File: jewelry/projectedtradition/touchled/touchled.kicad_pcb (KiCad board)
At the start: 2 copper layers, 23.6 x 23.6 mm, 18 parts, among them J3 SENSE, Q1 Q_NMOS_GSD, Q2 Q_NMOS_GSD, U1 TPP223-BA6, U2 AP3019A

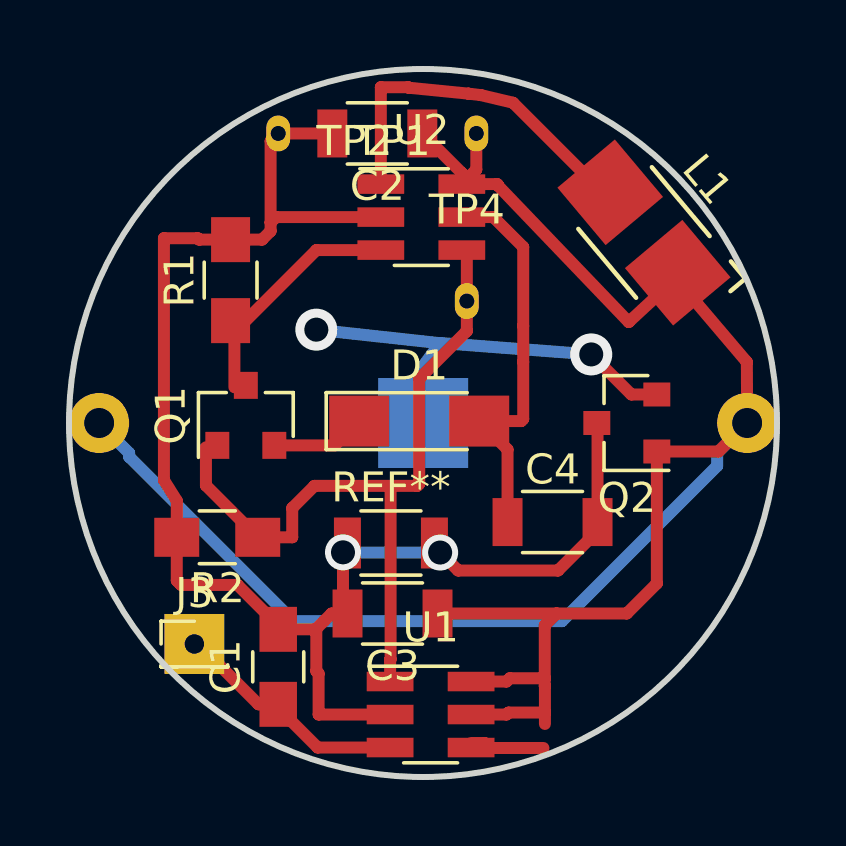
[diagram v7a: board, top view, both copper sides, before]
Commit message: jewelry: Fix transistor pinout
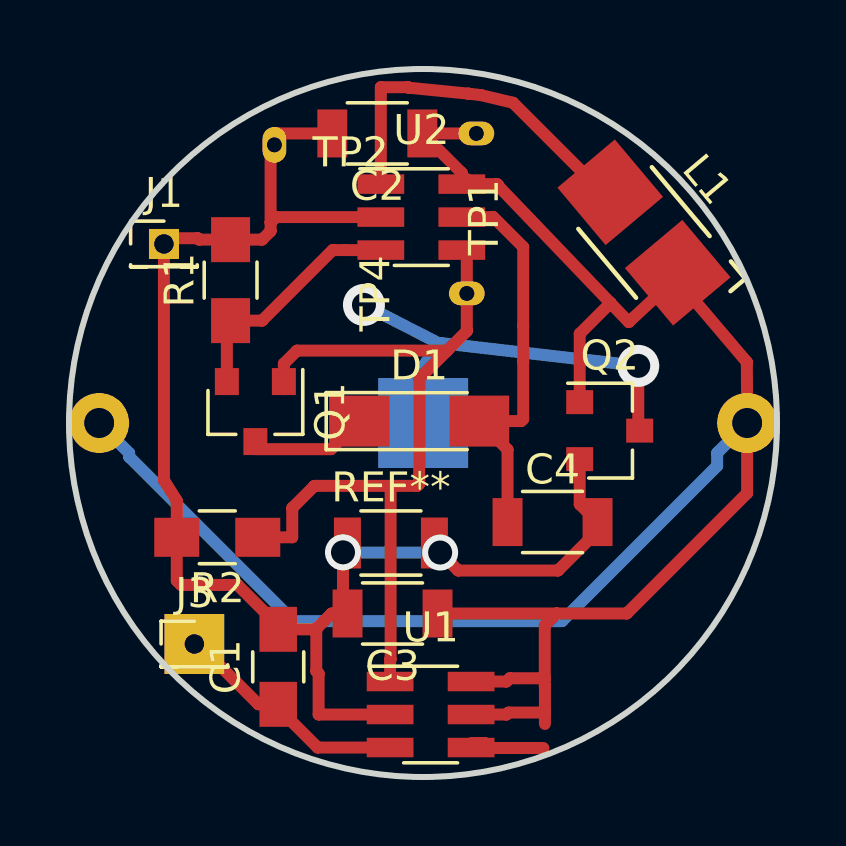
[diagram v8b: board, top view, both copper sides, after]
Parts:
- added J1: SENSEGND, Pin_Headers:Pin_Header_Straight_1x01_Pitch1.27mm, F.Cu at (-8.64, -5.97)
- Q1, Q2: value Q_NMOS_GSD -> BSS138L
- moved Q2 0.63 mm to (6.22, 0.25), turned to 0 degrees
- moved TP2 0.40 mm to (-4.95, -9.27)
- moved Q1 0.34 mm to (-5.59, -0.38), turned to 270 degrees
- moved TP4 0.25 mm to (1.46, -4.32), turned to 90 degrees
- turned TP1 to 270 degrees
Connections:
- Q1 pad 2: /LED- -> Net-(Q1-Pad2)
- Q1 pad 3: Net-(Q1-Pad3) -> /LED-
- Q2 pad 2: Net-(BT1-Pad2) -> GND
- Q2 pad 3: GND -> Net-(BT1-Pad2)
- R1 pad 1: Net-(Q1-Pad3) -> Net-(Q1-Pad2)
- U2 pad 3: Net-(Q1-Pad3) -> Net-(Q1-Pad2)
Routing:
- net Net-(Q1-Pad3): track 8.39 -> 0.00 mm
- net Net-(Q1-Pad2): track 0.00 -> 8.32 mm
- net touchon: track 25.6 -> 28.3 mm
- net VDD: track 71.5 -> 73.9 mm
- net GND: track 51.4 -> 50.4 mm
- net /LED-: track 3.16 -> 4.12 mm
